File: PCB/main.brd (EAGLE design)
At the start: 235.6 x 46 mm, 18 parts, among them IC1 DCDC, IC2 A4988BREAKOUT, IC3 A4988BREAKOUT, M1 NEAM17, M2 NEAM17

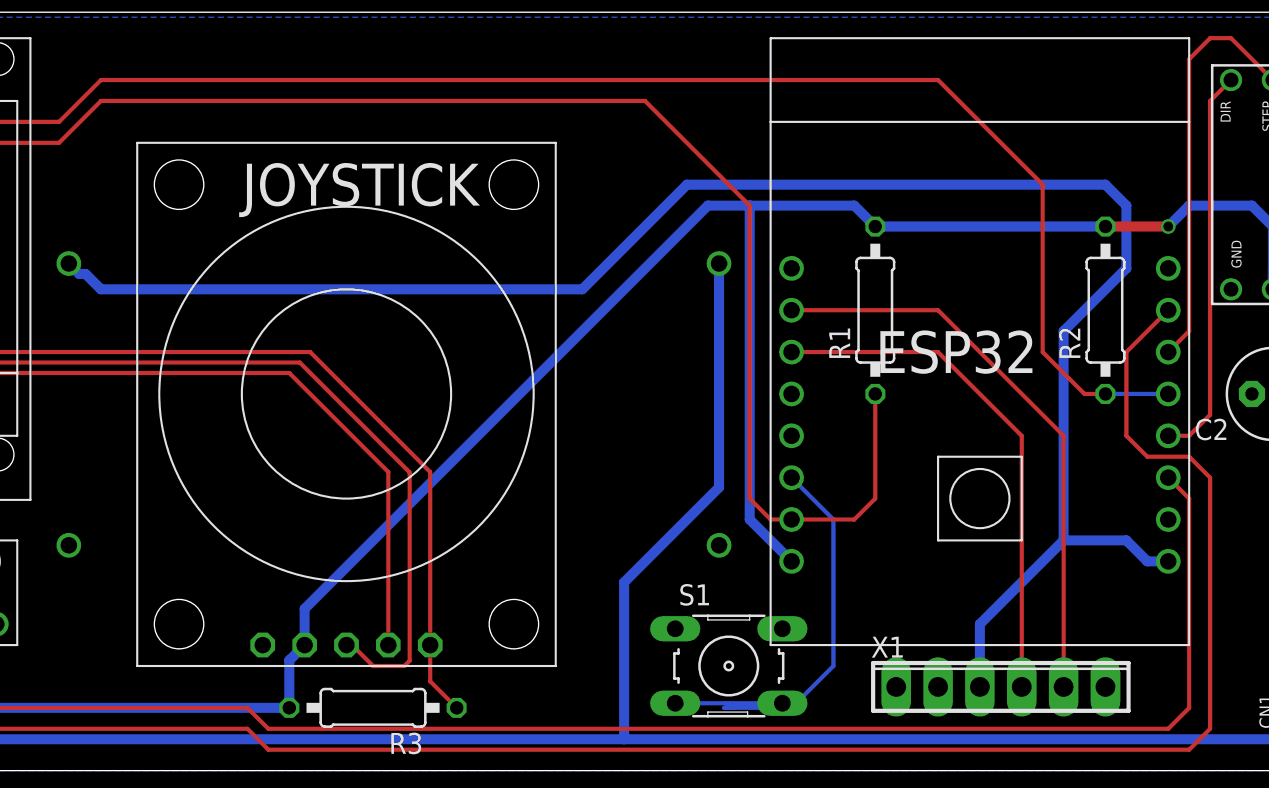
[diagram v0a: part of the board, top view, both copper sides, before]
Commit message: PIN 16 is used by PSRAM ...
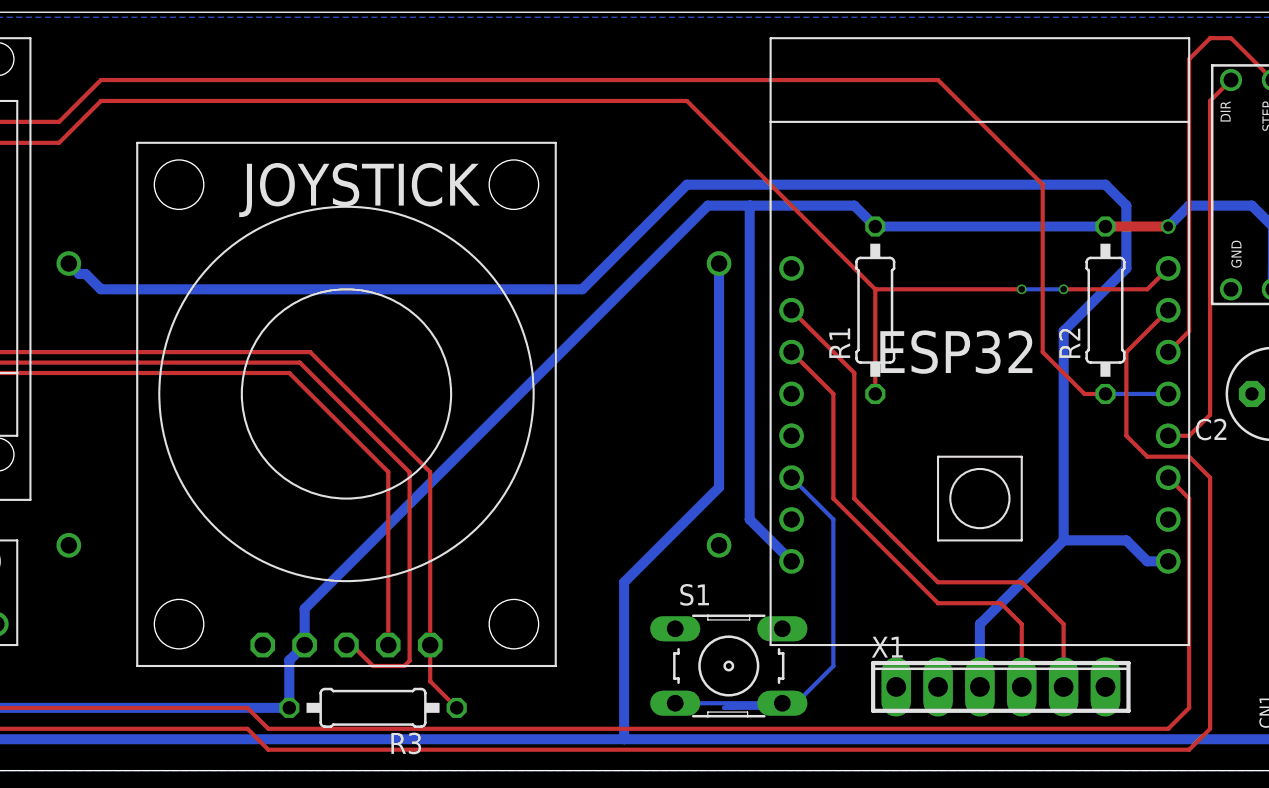
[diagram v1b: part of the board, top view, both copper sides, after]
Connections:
- net N$19: now also ESP32.GPIO4; no longer ESP32.GPIO16
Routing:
- net N$12: track 31.3 -> 28.3 mm
- net N$11: track 34.9 -> 32.7 mm
- net N$19: track 157.8 -> 159.3 mm, vias 0 -> 2
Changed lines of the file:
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@@
 <contactref element="X1" pad="5"/>
 <contactref element="ESP32" pad="GPIO1"/>
-<wire x1="160.02" y1="3.81" x2="160.02" y2="19.05" width="0.254" layer="1"/>
-<wire x1="160.02" y1="19.05" x2="152.4" y2="26.67" width="0.254" layer="1"/>
-<wire x1="152.4" y1="26.67" x2="143.51" y2="26.67" width="0.254" layer="1"/>
+<wire x1="160.02" y1="3.81" x2="160.02" y2="7.62" width="0.254" layer="1"/>
+<wire x1="160.02" y1="7.62" x2="157.48" y2="10.16" width="0.254" layer="1"/>
+<wire x1="157.48" y1="10.16" x2="152.4" y2="10.16" width="0.254" layer="1"/>
+<wire x1="152.4" y1="10.16" x2="147.32" y2="15.24" width="0.254" layer="1"/>
+<wire x1="147.32" y1="15.24" x2="147.32" y2="22.86" width="0.254" layer="1"/>
+<wire x1="147.32" y1="22.86" x2="143.51" y2="26.67" width="0.254" layer="1"/>
 </signal>
 <signal name="N$12">
 <contactref element="X1" pad="4"/>
 <contactref element="ESP32" pad="GPIO3"/>
-<wire x1="157.48" y1="3.81" x2="157.48" y2="19.05" width="0.254" layer="1"/>
-<wire x1="157.48" y1="19.05" x2="152.4" y2="24.13" width="0.254" layer="1"/>
-<wire x1="152.4" y1="24.13" x2="143.51" y2="24.13" width="0.254" layer="1"/>
+<wire x1="157.48" y1="3.81" x2="157.48" y2="7.62" width="0.254" layer="1"/>
+<wire x1="157.48" y1="7.62" x2="156.21" y2="8.89" width="0.254" layer="1"/>
+<wire x1="156.21" y1="8.89" x2="152.4" y2="8.89" width="0.254" layer="1"/>
+<wire x1="152.4" y1="8.89" x2="146.05" y2="15.24" width="0.254" layer="1"/>
+<wire x1="146.05" y1="15.24" x2="146.05" y2="21.59" width="0.254" layer="1"/>
+<wire x1="146.05" y1="21.59" x2="143.51" y2="24.13" width="0.254" layer="1"/>
 </signal>
 <signal name="STEP1">
@@
 <contactref element="ADC" pad="SDA"/>
 <contactref element="R1" pad="1"/>
-<contactref element="ESP32" pad="GPIO16"/>
 <wire x1="54.61" y1="34.29" x2="85.09" y2="34.29" width="0.254" layer="1"/>
 <wire x1="85.09" y1="34.29" x2="87.63" y2="36.83" width="0.254" layer="1"/>
@@
 <wire x1="87.63" y1="36.83" x2="99.06" y2="36.83" width="0.254" layer="1"/>
 <wire x1="99.06" y1="36.83" x2="101.6" y2="39.37" width="0.254" layer="1"/>
-<wire x1="148.59" y1="21.59" x2="148.59" y2="15.24" width="0.254" layer="1"/>
-<wire x1="148.59" y1="15.24" x2="147.32" y2="13.97" width="0.254" layer="1"/>
-<wire x1="147.32" y1="13.97" x2="143.51" y2="13.97" width="0.254" layer="1"/>
-<wire x1="101.6" y1="39.37" x2="134.62" y2="39.37" width="0.254" layer="1"/>
-<wire x1="134.62" y1="39.37" x2="140.97" y2="33.02" width="0.254" layer="1"/>
-<wire x1="140.97" y1="33.02" x2="140.97" y2="15.24" width="0.254" layer="1"/>
-<wire x1="140.97" y1="15.24" x2="142.24" y2="13.97" width="0.254" layer="1"/>
-<wire x1="142.24" y1="13.97" x2="143.51" y2="13.97" width="0.254" layer="1"/>
+<wire x1="101.6" y1="39.37" x2="137.16" y2="39.37" width="0.254" layer="1"/>
+<contactref element="ESP32" pad="GPIO4"/>
+<wire x1="137.16" y1="39.37" x2="148.59" y2="27.94" width="0.254" layer="1"/>
+<wire x1="148.59" y1="27.94" x2="148.59" y2="21.59" width="0.254" layer="1"/>
+<wire x1="148.59" y1="27.94" x2="157.48" y2="27.94" width="0.254" layer="1"/>
+<via x="157.48" y="27.94" extent="1-16" drill="0.4"/>
+<wire x1="157.48" y1="27.94" x2="160.02" y2="27.94" width="0.254" layer="16"/>
+<via x="160.02" y="27.94" extent="1-16" drill="0.4"/>
+<wire x1="160.02" y1="27.94" x2="165.1" y2="27.94" width="0.254" layer="1"/>
+<wire x1="165.1" y1="27.94" x2="166.37" y2="29.21" width="0.254" layer="1"/>
 </signal>
 </signals>

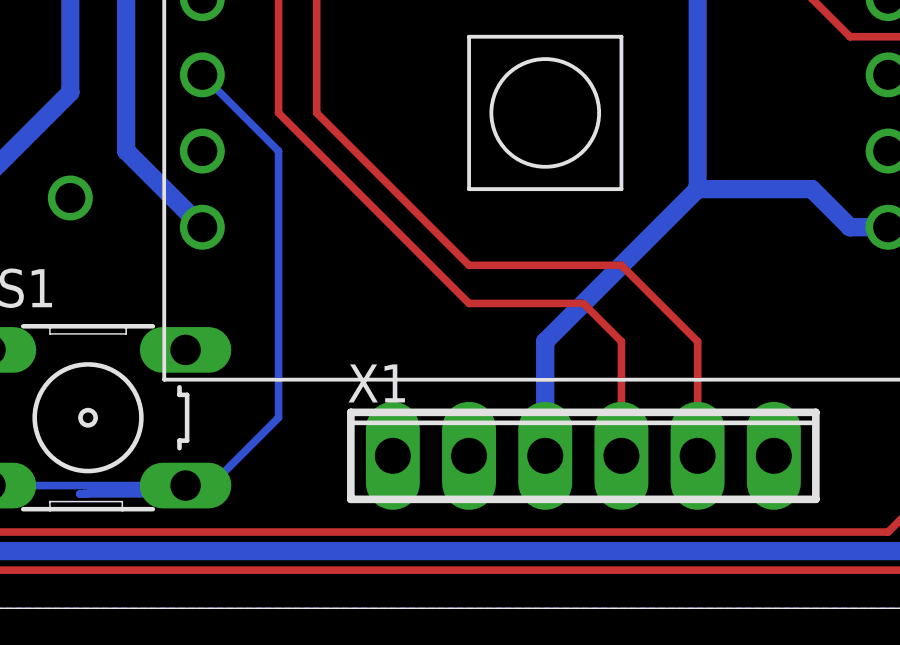
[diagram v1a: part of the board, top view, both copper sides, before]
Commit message: change debug port voltage to 3v3
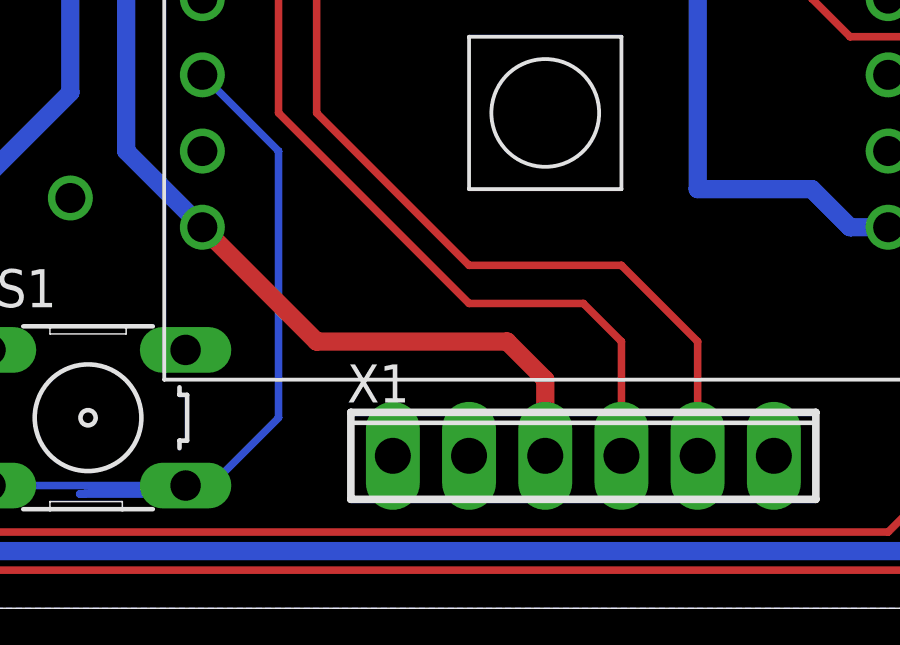
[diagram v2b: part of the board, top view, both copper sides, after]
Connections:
- net +3V3: now also X1.3
- net +5V: no longer X1.3
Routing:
- net +3V3: track 289.0 -> 305.1 mm
- net +5V: track 107.8 -> 96.8 mm
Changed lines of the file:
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@@
 <contactref element="IC1" pad="VOUT"/>
 <contactref element="ESP32" pad="5V"/>
-<contactref element="X1" pad="3"/>
 <wire x1="162.56" y1="34.29" x2="163.83" y2="33.02" width="0.6096" layer="16"/>
 <wire x1="163.83" y1="12.7" x2="165.1" y2="11.43" width="0.6096" layer="16"/>
 <wire x1="165.1" y1="11.43" x2="166.37" y2="11.43" width="0.6096" layer="16"/>
-<wire x1="154.94" y1="3.81" x2="154.94" y2="7.62" width="0.6096" layer="16"/>
-<wire x1="154.94" y1="7.62" x2="160.02" y2="12.7" width="0.6096" layer="16"/>
 <wire x1="163.83" y1="12.7" x2="160.02" y2="12.7" width="0.6096" layer="16"/>
 <wire x1="160.02" y1="12.7" x2="160.02" y2="25.4" width="0.6096" layer="16"/>
@@
 <wire x1="58.42" y1="6.35" x2="60.96" y2="8.89" width="0.254" layer="1"/>
 <wire x1="60.96" y1="8.89" x2="60.96" y2="15.24" width="0.254" layer="1"/>
+<contactref element="X1" pad="3"/>
+<wire x1="154.94" y1="3.81" x2="154.94" y2="6.35" width="0.6096" layer="1"/>
+<wire x1="154.94" y1="6.35" x2="153.67" y2="7.62" width="0.6096" layer="1"/>
+<wire x1="153.67" y1="7.62" x2="147.32" y2="7.62" width="0.6096" layer="1"/>
+<wire x1="147.32" y1="7.62" x2="143.51" y2="11.43" width="0.6096" layer="1"/>
 </signal>
 <signal name="N$2">

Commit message: Added missing ground connection on the jostick
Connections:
- net GND: now also JOYSTICK.GND
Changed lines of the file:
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@@
 <contactref element="C1" pad="-"/>
 <contactref element="C2" pad="-"/>
+<contactref element="JOYSTICK" pad="GND"/>
 </signal>
 <signal name="+12V">

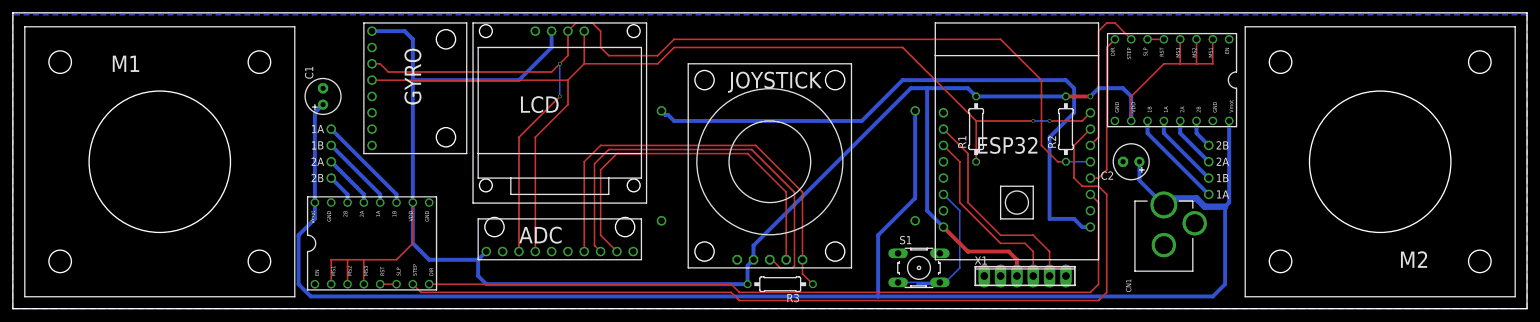
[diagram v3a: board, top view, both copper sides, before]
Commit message: lesson learned from prototype
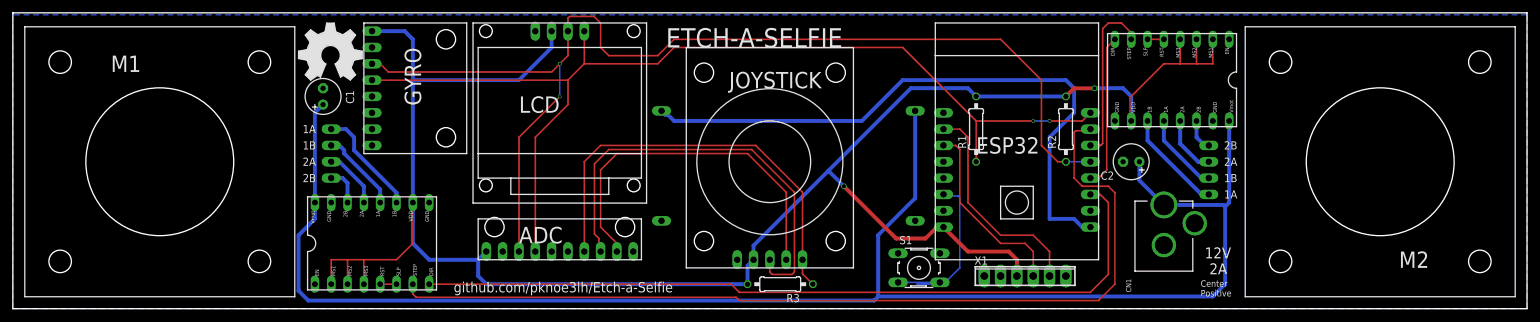
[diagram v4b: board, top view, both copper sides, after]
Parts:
- added LOGO1: OHW-LOGO_OSHW_LOGO_FILLX0350-NT, BBLeo_v2:OHW-LOGO_OSHW_FILLX350_NOTEXT
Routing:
- net STEP1: track 139.6 -> 143.6 mm
- net N$18: track 168.0 -> 170.8 mm
- net N$15: track 64.8 -> 67.3 mm
- net DIR1: track 119.7 -> 121.8 mm
- net N$11: track 32.7 -> 34.2 mm
- net STEP2: track 25.0 -> 26.3 mm
- net N$1: track 15.6 -> 17.0 mm
- net N$13: track 30.2 -> 31.4 mm
- net N$12: track 28.3 -> 29.5 mm
- net N$3: track 4.86 -> 5.90 mm
- net N$8: track 8.19 -> 9.16 mm
- net N$4: track 8.45 -> 9.20 mm
- net N$5: track 12.0 -> 12.8 mm
- net N$10: track 15.4 -> 16.0 mm
- net N$9: track 11.8 -> 12.5 mm
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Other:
- board text added: "12V"
- board text added: "2A"
- board text added: "Center Positive"
- board text added: "ETCH-A-SELFIE"
- board text added: "github.com/pknoe3lh/Etch-a-Selfie"
